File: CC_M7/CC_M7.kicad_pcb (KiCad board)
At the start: 4 copper layers, 40 x 65 mm, 136 parts, among them J1 Conn_01x04_Pin, J10 Conn_01x04_Pin, J11 USB_B_Micro, J12 Conn_01x04_Pin, J13 Batt_Pins, J3 Conn_01x03_Pin, J4 Conn_01x03_Pin, J5 Conn_01x03_Pin, J6 Conn_01x03_Pin, J7 Conn_01x03_Pin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

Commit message: Routing Update
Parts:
- moved R7 12.1 mm to (98.7, 146.3), turned to 0 degrees
- moved U9 0.71 mm to (105.7, 164.9)
- moved U2 0.06 mm to (97.9, 126.4)
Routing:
- net +3.3V: track 84.3 -> 95.7 mm, vias 32 -> 34
- net GND: track 61.9 -> 73.0 mm
- net USB_DM: track 46.7 -> 53.4 mm, vias 3 -> 2
- net USB_DP: track 49.0 -> 53.9 mm, vias 4 -> 3
- net UART2_RX: track 29.3 -> 26.1 mm
- net PA1: track 22.9 -> 19.7 mm
- net UART2_TX: track 25.3 -> 22.6 mm
- net PA0: track 25.1 -> 22.5 mm
- net NRF_SPI0_CS: track 14.9 -> 17.5 mm, vias 2 -> 3
- net 3V3_RF: track 77.9 -> 79.8 mm
- net DEC4: track 15.3 -> 14.6 mm

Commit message: last check
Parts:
- C28, C29, C58: footprint Capacitor_SMD:C_0402_1005Metric -> Capacitor_SMD:C_0201_0603Metric
- L6, L7: footprint Inductor_SMD:L_0402_1005Metric -> Inductor_SMD:L_0201_0603Metric
- moved C29 0.84 mm to (118.7, 124.5), turned to -90 degrees
- moved L7 0.66 mm to (118.4, 123.3)
- moved L6 0.62 mm to (117.3, 123.0), turned to -90 degrees
- moved C28 0.49 mm to (118.1, 122.2), turned to 90 degrees
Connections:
- net USB_DM renamed USB_DN
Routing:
- net USB_DN: track 53.4 -> 51.2 mm
- net USB_DP: track 53.9 -> 55.7 mm
- net NRST: track 55.9 -> 54.6 mm
- net Net-(C28-Pad1): track 2.37 -> 1.60 mm
- net Net-(C29-Pad1): track 5.63 -> 4.95 mm

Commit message: ...
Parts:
- added C61: 1pF, Capacitor_SMD:C_0201_0603Metric, F.Cu at (108.3, 104.3)
- added C62: 1.2pF, Capacitor_SMD:C_0201_0603Metric, F.Cu at (109.8, 104.3)
- added L2: 4.7nH, Inductor_SMD:L_0201_0603Metric, F.Cu at (108.3, 103.6)
- added L3: 2.2nH, Inductor_SMD:L_0201_0603Metric, F.Cu at (109.8, 103.6)
- D9: value SS210 -> B5819WS
- moved C40 20.2 mm to (81.6, 122.8)
- moved C11 19.8 mm to (82.6, 120.6)
- moved C31 4.10 mm to (107.4, 117.0)
- moved U6 1.86 mm to (104.6, 122.4)
- moved C32 1.86 mm to (105.6, 114.1)
- moved C33 1.86 mm to (100.3, 120.2)
- moved C38 1.86 mm to (100.4, 119.2)
- moved C41 1.86 mm to (100.4, 118.3)
- moved C44 1.86 mm to (103.2, 114.1)
- moved Y2 1.86 mm to (104.5, 116.3)
- moved C36 1.15 mm to (108.4, 117.0), turned to 90 degrees
- moved JP1 0.93 mm to (96.1, 119.8)
- moved JP10 0.93 mm to (99.0, 125.4)
- moved JP2 0.93 mm to (96.1, 121.2)
- moved JP3 0.93 mm to (96.1, 122.6)
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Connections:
- U6 pad 24: NRF_ANT -> Net-(U6-ANT)
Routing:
- net 3V3_RF: track 79.8 -> 43.0 mm, vias 8 -> 6
- net +3.3V: track 95.7 -> 80.6 mm, vias 34 -> 30
- net GND: track 73.0 -> 59.6 mm, vias 61 -> 58
- net NRF_NRST: track 9.24 -> 0.56 mm, vias 2 -> 1
- net DEC3: track 2.56 -> 5.37 mm
- net NRF_SWDIO: track 12.6 -> 10.0 mm
- net NRF_SWCLK: track 12.8 -> 10.3 mm
- net NRF_ANT: track 2.22 -> 0.00 mm
- net NRF_PA_TX_EN: track 8.07 -> 10.2 mm
- net NRF_PA_RX_EN: track 8.11 -> 10.2 mm
- net NRF_PA_MODE: track 11.7 -> 13.6 mm
- net NRF_LED1: track 9.65 -> 7.79 mm
- net NRF_PA_PDN: track 7.33 -> 9.19 mm
- net NRF_SPI0_CS: track 17.5 -> 19.3 mm
- net NRF_LED0: track 11.2 -> 9.41 mm
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
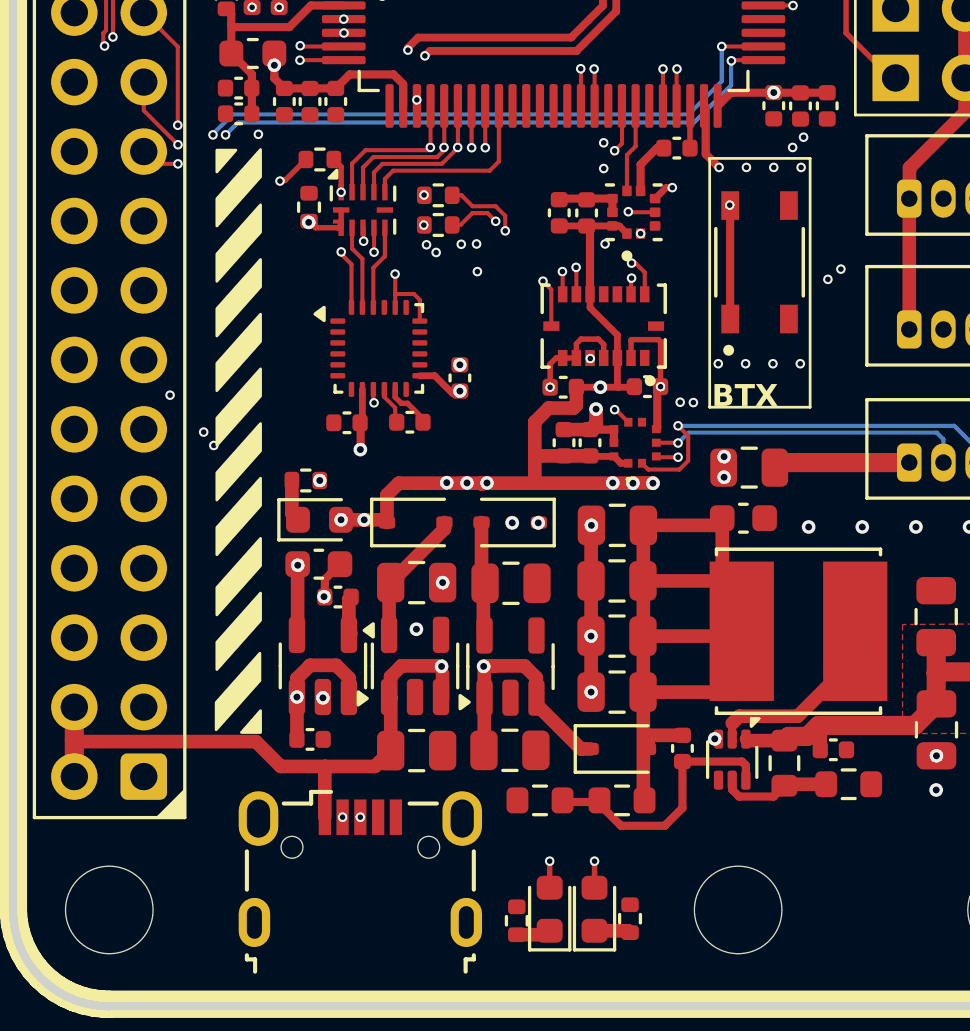
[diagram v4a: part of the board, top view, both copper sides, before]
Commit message: vias constraints changes
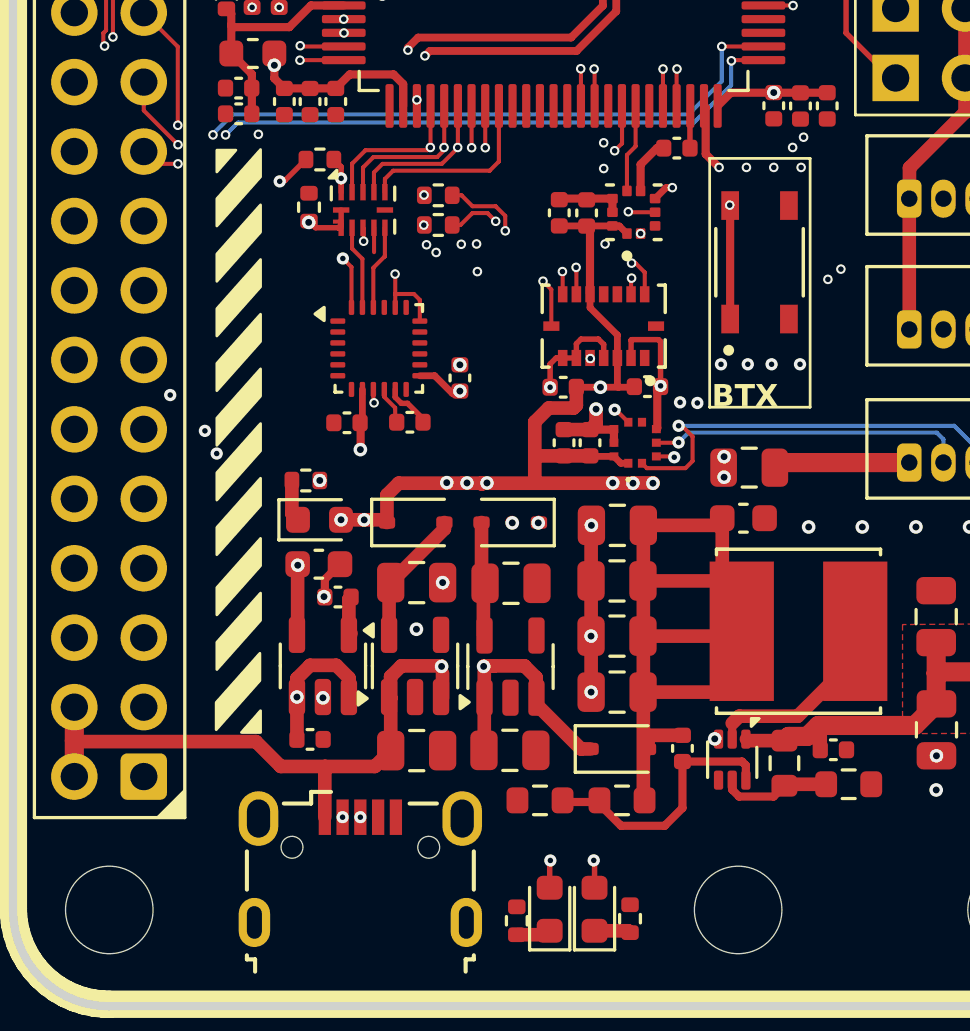
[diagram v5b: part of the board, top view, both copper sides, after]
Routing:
- net SPI1_MOSI_1V8: track 4.29 -> 4.05 mm, vias 2 -> 1

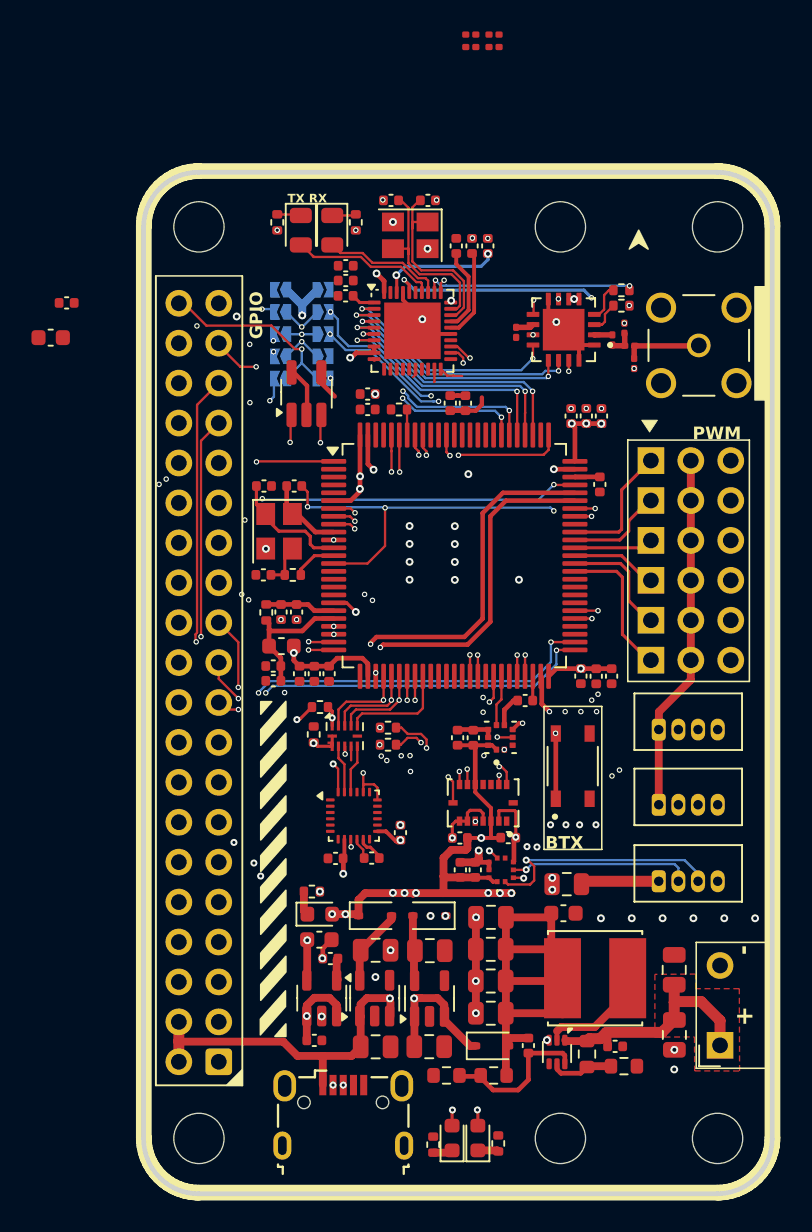
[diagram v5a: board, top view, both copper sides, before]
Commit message: via correction completed
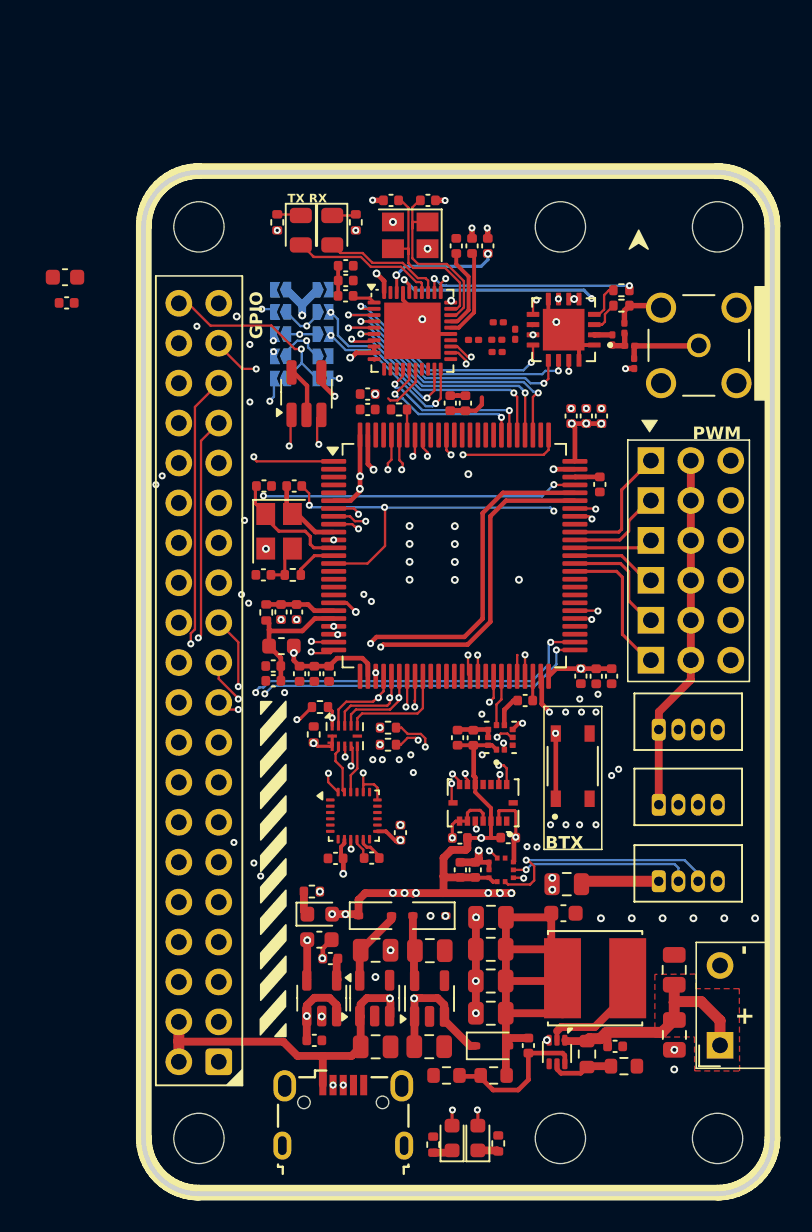
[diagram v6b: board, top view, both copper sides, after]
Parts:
- moved C61 19.5 mm to (110.0, 123.8)
- moved L2 19.4 mm to (108.5, 123.0)
- moved L3 19.4 mm to (110.0, 123.0)
- moved C62 17.5 mm to (110.1, 121.9)
- moved C40 3.95 mm to (82.5, 119.0)
- moved C58 0.13 mm to (111.1, 122.6)
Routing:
- net GND: track 59.5 -> 68.0 mm, vias 58 -> 55
- net NRF_NRST: track 0.56 -> 4.07 mm
- net SPI3_IRQ: track 7.92 -> 10.8 mm
- net PC14: track 24.4 -> 26.3 mm
- net SPI3_CS: track 8.92 -> 10.6 mm
- net SPI3_SCK: track 16.7 -> 18.3 mm
- net SPI1_CS2: track 14.7 -> 16.3 mm
- net PC13: track 21.6 -> 23.1 mm
- net NRF_SWDIO: track 10.0 -> 11.2 mm
- net Net-(U7-TRX): track 1.20 -> 0.05 mm
- net UART3_TX: track 13.4 -> 14.5 mm
- net NRF_SPI0_MISO: track 16.3 -> 17.3 mm
- net J2_36: track 12.5 -> 13.3 mm
- net NRF_SWCLK: track 10.3 -> 11.1 mm
- net I2C1_SCL: track 62.5 -> 63.2 mm
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
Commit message: CCM7 Unconnected item routing progress.
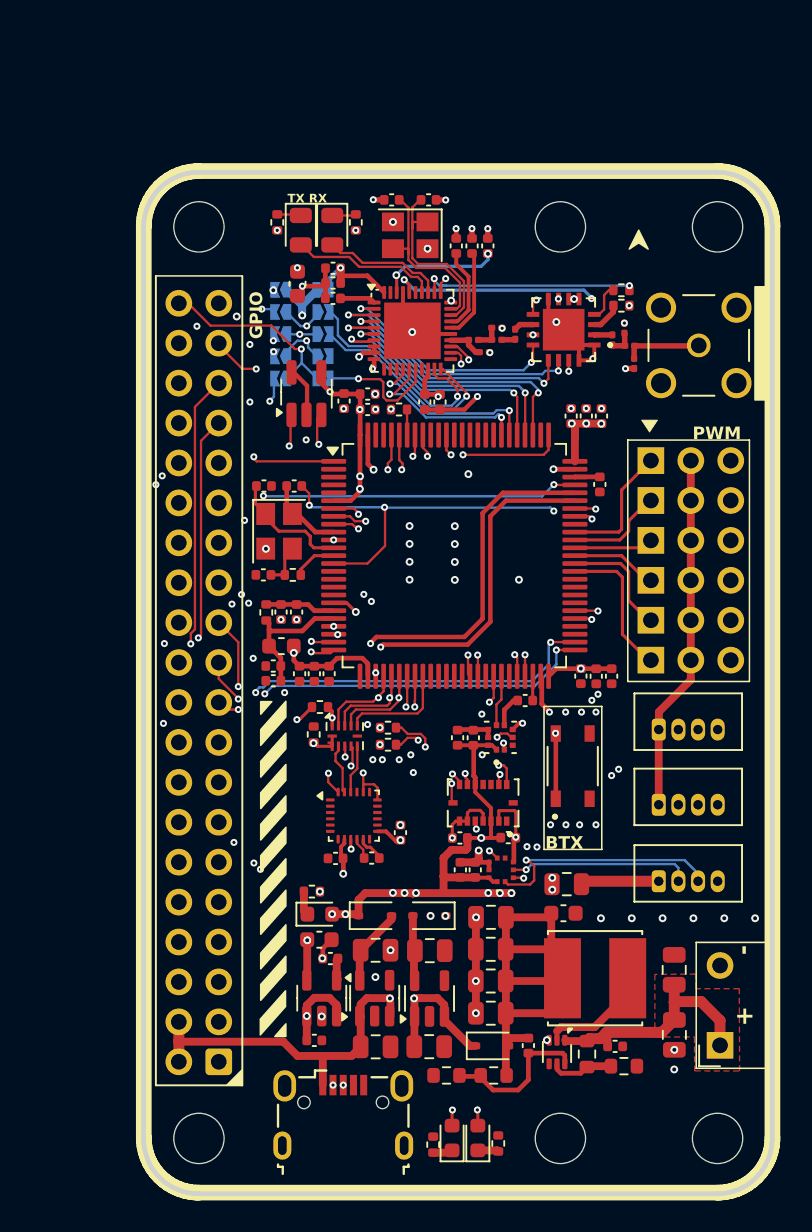
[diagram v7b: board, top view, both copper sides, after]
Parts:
- moved C11 18.7 mm to (100.2, 126.9), turned to -90 degrees
- moved C40 14.8 mm to (97.3, 119.4), turned to 90 degrees
- moved C39 1.62 mm to (105.4, 126.9)
- moved C42 1.62 mm to (106.4, 126.9)
- moved C38 0.82 mm to (99.6, 119.4)
- moved C33 0.82 mm to (99.5, 120.3)
- moved C41 0.82 mm to (99.5, 118.4)
- moved C61 0.81 mm to (109.2, 123.8)
- moved C62 0.36 mm to (110.0, 122.2)
- moved C44 0.05 mm to (103.3, 114.1)
- moved C32 0.05 mm to (105.6, 114.1)
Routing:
- net 3V3_RF: track 43.0 -> 78.2 mm, vias 6 -> 8
- net +3.3V: track 80.6 -> 95.5 mm, vias 31 -> 33
- net NRF_NRST: track 4.07 -> 8.26 mm
- net GND: track 68.0 -> 71.9 mm, vias 55 -> 73
- net NRF_SWDIO: track 11.2 -> 14.2 mm, vias 2 -> 1
- net NRF_SWCLK: track 11.1 -> 13.6 mm, vias 2 -> 1
- net Net-(U6-ANT): track 0.00 -> 2.34 mm
- net Net-(C62-Pad1): track 0.00 -> 1.60 mm
- net Net-(U7-TRX): track 0.05 -> 1.31 mm
- net UART3_TX: track 14.5 -> 13.4 mm
- net SPI3_CS: track 10.6 -> 11.4 mm
- net NRF_ANT: track 0.00 -> 0.86 mm
- net SPI3_IRQ: track 10.8 -> 11.6 mm
- net DEC1: track 1.51 -> 2.25 mm
- net I2C2_SCL: track 40.5 -> 40.6 mm, vias 2 -> 3
